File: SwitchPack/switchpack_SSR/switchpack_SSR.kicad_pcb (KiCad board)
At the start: 2 copper layers, 12 parts, among them J1 OUT_DIP_LEFT, J2 GND, J3 IN_DIP_LEFT, J4 GND, J5 VBAT_DIP_LEFT, U1 VN7003ALH

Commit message: Update switchpack
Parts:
- added C2: 100n, Yame_library:SM0402-MR, F.Cu at (126.2, -6.30)
- added C3: 100n, Yame_library:SM0402-MR, F.Cu at (133.0, -13.2)
- added C4: 100n, Yame_library:SM0402-MR, F.Cu at (144.9, -28.7)
- added C5: 100n, Yame_library:SM0402-MR, F.Cu at (149.3, -31.7)
- added C6: 100n, Yame_library:SM0402-MR, F.Cu at (128.6, -9.72)
- added C7: 100n, Yame_library:SM0402-MR, F.Cu at (133.0, -15.8)
- added C8: 22u, Yame_library:SM0805-MR, F.Cu at (186.1, -37.7)
- added D2: LED, LED_SMD:LED_0805_2012Metric, F.Cu at (128.7, -15.6)
- added D3: LED, LED_SMD:LED_0805_2012Metric, F.Cu at (145.0, -31.5)
- added D4: LED, LED_SMD:LED_0805_2012Metric, F.Cu at (128.7, -12.5)
- added D5: LED, LED_SMD:LED_0805_2012Metric, F.Cu at (133.2, -18.6)
- added D6: LED, LED_SMD:LED_0805_2012Metric, F.Cu at (128.7, -18.6)
- added D7: LED, LED_SMD:LED_0805_2012Metric, F.Cu at (137.6, -18.6)
- added D8: D_Schottky, Diode_SMD:D_SOD-123F, F.Cu at (186.8, -49.0)
- added J10: OUT_AC_REC, Connector_Wire:SolderWire-2.5sqmm_1x01_D2.4mm_OD4.4mm, F.Cu at (131.2, 103.5)
- added J11: IN_AC_REC, Connector_Pin:Pin_D0.7mm_L6.5mm_W1.8mm_FlatFork, F.Cu at (121.1, 112.4)
- added J12: VBAT_MB_LEFT, Connector_Wire:SolderWire-2.5sqmm_1x01_D2.4mm_OD4.4mm, F.Cu at (159.2, 72.0)
- added J13: VBAT_PARKING_LIGHT, Connector_Wire:SolderWire-2.5sqmm_1x01_D2.4mm_OD4.4mm, F.Cu at (141.8, 119.5)
- added J14: OUT_DIP_RIGHT, Connector_Wire:SolderWire-2.5sqmm_1x01_D2.4mm_OD4.4mm, F.Cu at (131.2, 128.4)
- added J15: OUT_MB_RIGHT, Connector_Wire:SolderWire-2.5sqmm_1x01_D2.4mm_OD4.4mm, F.Cu at (125.2, 74.7)
- added J16: OUT_FOG_LIGHT, Connector_Wire:SolderWire-2.5sqmm_1x01_D2.4mm_OD4.4mm, F.Cu at (136.9, 104.0)
- added J17: IN_DIP_RIGHT, Connector_Pin:Pin_D0.7mm_L6.5mm_W1.8mm_FlatFork, F.Cu at (121.1, 119.5)
- added J18: IN_MB_RIGHT, Connector_Pin:Pin_D0.7mm_L6.5mm_W1.8mm_FlatFork, F.Cu at (125.2, 80.7)
- added J19: IN_FOG_LIGHT, Connector_Pin:Pin_D0.7mm_L6.5mm_W1.8mm_FlatFork, F.Cu at (147.1, 112.8)
- added J20: VBAT_AC_REC, Connector_Wire:SolderWire-2.5sqmm_1x01_D2.4mm_OD4.4mm, F.Cu at (126.2, 112.4)
- added J21: VBAT_DIP_RIGHT, Connector_Wire:SolderWire-2.5sqmm_1x01_D2.4mm_OD4.4mm, F.Cu at (126.2, 119.5)
- added J22: VBAT_MB_RIGHT, Connector_Wire:SolderWire-2.5sqmm_1x01_D2.4mm_OD4.4mm, F.Cu at (137.2, 77.0)
- added J23: VBAT_FOG_LIGHT, Connector_Wire:SolderWire-2.5sqmm_1x01_D2.4mm_OD4.4mm, F.Cu at (142.1, 112.8)
- added J24: +3.3V, Connector_Pin:Pin_D0.7mm_L6.5mm_W1.8mm_FlatFork, F.Cu at (191.2, -13.6)
- added J25: +12V, Connector_Pin:Pin_D0.7mm_L6.5mm_W1.8mm_FlatFork, F.Cu at (196.6, -23.6)
- added J6: OUT_MB_LEFT, Connector_Wire:SolderWire-2.5sqmm_1x01_D2.4mm_OD4.4mm, F.Cu at (147.1, 69.7)
- added J7: OUT_PARKING_LIGHT, Connector_Wire:SolderWire-2.5sqmm_1x01_D2.4mm_OD4.4mm, F.Cu at (136.7, 128.4)
- added J8: IN_MB_LEFT, Connector_Pin:Pin_D0.7mm_L6.5mm_W1.8mm_FlatFork, F.Cu at (147.1, 75.7)
- added J9: IN_PARKING_LIGHT, Connector_Pin:Pin_D0.7mm_L6.5mm_W1.8mm_FlatFork, F.Cu at (146.8, 119.5)
- added Q1: DTC143Z, Package_TO_SOT_SMD:SOT-323_SC-70, F.Cu at (186.3, -40.9)
- added Q2: DTC143Z, Package_TO_SOT_SMD:SOT-323_SC-70, F.Cu at (191.1, -44.2)
- added Q3: DTC143Z, Package_TO_SOT_SMD:SOT-323_SC-70, F.Cu at (196.6, -48.8)
- added Q4: DTC143Z, Package_TO_SOT_SMD:SOT-323_SC-70, F.Cu at (190.7, -40.6)
- added Q5: DTC143Z, Package_TO_SOT_SMD:SOT-323_SC-70, F.Cu at (195.2, -40.6)
- added Q6: DTC143Z, Package_TO_SOT_SMD:SOT-323_SC-70, F.Cu at (201.1, -48.8)
- added Q7: DTC143Z, Package_TO_SOT_SMD:SOT-323_SC-70, F.Cu at (195.6, -44.2)
- added R10: 1k, Yame_library:SM0402-MR, F.Cu at (133.0, -10.6)
- added R11: 1k, Yame_library:SM0402-MR, F.Cu at (126.2, -3.68)
- added R12: 15k, Yame_library:SM0402-MR, F.Cu at (153.5, -31.7)
- added R13: 15k, Yame_library:SM0402-MR, F.Cu at (130.3, -7.10)
- added R14: 15k, Yame_library:SM0402-MR, F.Cu at (137.2, -13.2)
- added R15: 1k, Yame_library:SM0402-MR, F.Cu at (153.5, -29.1)
- added R16: 1k, Yame_library:SM0402-MR, F.Cu at (149.3, -29.1)
- added R17: 1k, Yame_library:SM0402-MR, F.Cu at (141.3, -15.8)
- added R18: 15k, Yame_library:SM0402-MR, F.Cu at (134.5, -7.94)
- added R19: 15k, Yame_library:SM0402-MR, F.Cu at (134.5, -5.32)
- added R20: 15k, Yame_library:SM0402-MR, F.Cu at (137.2, -15.8)
- added R21: 1k, Yame_library:SM0402-MR, F.Cu at (146.1, -18.2)
- added R22: 15k, Yame_library:SM0402-MR, F.Cu at (141.3, -13.2)
- added R23: 1k, Yame_library:SM0402-MR, F.Cu at (126.2, -1.06)
- added R24: 1k, Yame_library:SM0402-MR, F.Cu at (130.3, -4.48)
- added R25: 1k, Yame_library:SM0402-MR, F.Cu at (137.2, -10.6)
- added R26: 15k, Yame_library:SM0402-MR, F.Cu at (153.2, -26.5)
- added R27: 15k, Yame_library:SM0402-MR, F.Cu at (146.1, -20.8)
- added R28: 15k, Yame_library:SM0402-MR, F.Cu at (149.0, -23.9)
- added R29: 15k, Yame_library:SM0402-MR, F.Cu at (190.3, -37.4)
- added R30: 15k, Yame_library:SM0402-MR, F.Cu at (199.9, -45.7)
- added R31: 15k, Yame_library:SM0402-MR, F.Cu at (205.4, -49.3)
- added R32: 15k, Yame_library:SM0402-MR, F.Cu at (194.4, -37.4)
- added R33: 15k, Yame_library:SM0402-MR, F.Cu at (199.9, -43.1)
- added R34: 15k, Yame_library:SM0402-MR, F.Cu at (204.0, -45.7)
- added R35: 15k, Yame_library:SM0402-MR, F.Cu at (199.5, -40.4)
- added R5: 1k, Yame_library:SM0402-MR, F.Cu at (130.3, -1.86)
- added R6: 1k, Yame_library:SM0402-MR, F.Cu at (144.9, -26.1)
- added R7: 15k, Yame_library:SM0402-MR, F.Cu at (144.9, -23.5)
- added R8: 15k, Yame_library:SM0402-MR, F.Cu at (141.9, -18.8)
- added R9: 1k, Yame_library:SM0402-MR, F.Cu at (149.0, -26.5)
- added U2: VN7003ALH, Yame_library:VN7003ALH, B.Cu at (152.1, 82.8)
- added U3: VN7003ALH, Yame_library:VN7003ALH, B.Cu at (149.0, 128.2)
- added U4: VN7003ALH, Yame_library:VN7003ALH, B.Cu at (124.2, 103.8)
- added U5: VN7003ALH, Yame_library:VN7003ALH, B.Cu at (119.3, 127.5)
- added U6: VN7003ALH, Yame_library:VN7003ALH, B.Cu at (134.7, 87.8)
- added U7: VN7003ALH, Yame_library:VN7003ALH, B.Cu at (152.7, 105.7)
- C1, R1, R2, R3, R4: footprint Yame_library:SM0805-MR -> Yame_library:SM0402-MR
- J2, J4: footprint Connector_Wire:SolderWire-0.75sqmm_1x01_D1.25mm_OD2.3mm -> Connector_Pin:Pin_D0.7mm_L6.5mm_W1.8mm_FlatFork
- U1: moved to B.Cu
- moved J5 89.0 mm to (177.2, 80.3)
- moved U1 85.8 mm to (167.8, 82.5), turned to 90 degrees
- moved J1 78.6 mm to (168.3, 75.2)
- moved J3 76.8 mm to (177.2, 75.3)
- moved C1 59.9 mm to (169.5, 54.2)
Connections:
- R2 pad 2: Net-(J3-Pad1) -> +3V3
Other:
- board text added: "AC+"
- board text added: "ACin"
- board text added: "ACout"
- board text added: "B-"
- board text added: "DipL"
- board text added: "DipLin"
- board text added: "DipLout"
- board text added: "DipR"
- board text added: "DipRIn"
- board text added: "DipRout"
- board text added: "Fog+"
- board text added: "FogIn"
- board text added: "FogOut"
- board text added: "MBL+"
- board text added: "MBLin"
- board text added: "MBLout"
- board text added: "MBR+"
- board text added: "MBRin"
- board text added: "MBRout"
- board text added: "Park+"
- board text added: "Parkin"
- board text added: "Parkout"

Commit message: SwitchPack : update layout
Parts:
- removed D8: D_Schottky, Diode_SMD:D_SOD-123F
- added R36: 0R, Yame_library:SM0402-MR, F.Cu at (202.8, 103.0)
- C5, R23, R26: moved to B.Cu
- moved Q3 199.5 mm to (142.9, 143.3)
- moved R31 193.1 mm to (146.7, 134.7)
- moved R33 178.4 mm to (121.1, 117.0), turned to 90 degrees
- moved Q5 177.6 mm to (115.9, 118.4), turned to 180 degrees
- moved D3 169.6 mm to (147.3, 138.1)
- moved C5 165.1 mm to (124.6, 131.6)
- moved R6 163.5 mm to (140.6, 137.3)
- moved R15 162.7 mm to (132.8, 132.3), turned to 180 degrees
- moved C3 158.8 mm to (153.3, 144.3)
- moved R26 158.1 mm to (127.2, 129.4)
- moved D5 150.8 mm to (129.7, 132.2)
- moved J25 148.9 mm to (136.9, 112.8)
- moved R11 143.0 mm to (154.9, 136.4)
- moved R13 142.6 mm to (156.7, 133.1)
- moved J24 140.3 mm to (152.1, 121.1)
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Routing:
- net Net-(C3-Pad1): track 0.00 -> 14.8 mm
- net Net-(C5-Pad1): track 0.00 -> 14.4 mm
- net Net-(J7-Pad1): track 0.00 -> 12.9 mm
- net Net-(J14-Pad1): track 0.00 -> 9.50 mm
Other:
- board outline added: 68.2 x 78.8 mm
- copper layers 2 -> 4

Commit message: switchpack : update layout
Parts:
- C1, C2, C3, C4, C6, C7, R10, R11, R12, R13, R21, R22, R24, R25, R27, R28, R3, R4: moved to B.Cu
- moved Q4 170.4 mm to (116.9, 113.0), turned to 180 degrees
- moved R32 169.2 mm to (119.0, 114.1), turned to 270 degrees
- moved Q7 164.3 mm to (151.1, 114.0)
- moved R35 161.5 mm to (148.9, 113.0), turned to 90 degrees
- moved C8 161.4 mm to (157.4, 121.0)
- moved Q6 156.7 mm to (120.8, 85.8)
- moved R34 155.9 mm to (118.6, 84.7), turned to 90 degrees
- moved C4 137.4 mm to (129.6, 107.8)
- moved R30 136.4 mm to (142.1, 77.8), turned to 90 degrees
- moved R9 135.4 mm to (133.2, 108.0), turned to 270 degrees
- moved Q2 131.8 mm to (144.2, 79.0)
- moved R20 131.2 mm to (153.2, 114.5), turned to 270 degrees
- moved D7 128.8 mm to (135.8, 110.2), turned to 180 degrees
- moved J2 128.0 mm to (175.1, 119.9)
- moved R14 127.7 mm to (114.7, 112.5), turned to 90 degrees
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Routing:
- net +12V: track 0.00 -> 182.3 mm
- net +3V3: track 0.00 -> 176.9 mm, vias 0 -> 4
- net GND: track 0.00 -> 73.7 mm, vias 0 -> 31
- net Net-(J16-Pad1): track 0.00 -> 29.3 mm
- net Net-(J1-Pad1): track 0.00 -> 25.8 mm
- net Net-(J10-Pad1): track 0.00 -> 25.6 mm
- net Net-(C2-Pad1): track 0.00 -> 22.3 mm, vias 0 -> 64
- net Net-(C6-Pad1): track 0.00 -> 22.3 mm, vias 0 -> 64
- net Net-(Q5-Pad3): track 0.00 -> 21.6 mm, vias 0 -> 1
- net Net-(C1-Pad1): track 0.00 -> 21.5 mm, vias 0 -> 64
- net Net-(C4-Pad1): track 0.00 -> 21.3 mm, vias 0 -> 64
- net Net-(C7-Pad1): track 0.00 -> 21.1 mm, vias 0 -> 64
- net Net-(Q7-Pad3): track 0.00 -> 21.0 mm, vias 0 -> 1
- net Net-(Q4-Pad3): track 0.00 -> 20.6 mm, vias 0 -> 1
- net Net-(J6-Pad1): track 0.00 -> 20.6 mm
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- added copper zone on B.Cu, net GND
- added copper zone on F.Cu, net GND
- added copper zone on B.Cu, net Net-(C1-Pad1)
- added copper zone on F.Cu, net Net-(C1-Pad1)
- added copper zone on B.Cu, net Net-(C2-Pad1)
- added copper zone on F.Cu, net Net-(C2-Pad1)
- added copper zone on B.Cu, net Net-(C3-Pad1)
- added copper zone on F.Cu, net Net-(C3-Pad1)
- added copper zone on B.Cu, net Net-(C4-Pad1)
- added copper zone on F.Cu, net Net-(C4-Pad1)
- added copper zone on B.Cu, net Net-(C5-Pad1)
- added copper zone on F.Cu, net Net-(C5-Pad1)
- added copper zone on B.Cu, net Net-(C6-Pad1)
- added copper zone on F.Cu, net Net-(C6-Pad1)
- added copper zone on B.Cu, net Net-(C7-Pad1)
- added copper zone on F.Cu, net Net-(C7-Pad1)
- added copper zone on B.Cu, net Net-(J1-Pad1)
- added copper zone on B.Cu, net Net-(J10-Pad1)
- added copper zone on B.Cu, net Net-(J14-Pad1)
- added copper zone on B.Cu, net Net-(J15-Pad1)
- added copper zone on B.Cu, net Net-(J16-Pad1)
- added copper zone on B.Cu, net Net-(J6-Pad1)
- added copper zone on B.Cu, net Net-(J7-Pad1)
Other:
- copper layers 4 -> 2
- net class Default: clearance 0.2 -> 0.15; trace_width 0.25 -> 0.15; via_dia 0.8 -> 0.4; via_drill 0.4 -> 0.2
- rule trace_clearance: 0.2 -> 0.15
- rule trace_min: 0.2 -> 0.15
- rule via_min_drill: 0.3 -> 0.1
- rule via_min_size: 0.4 -> 0.2

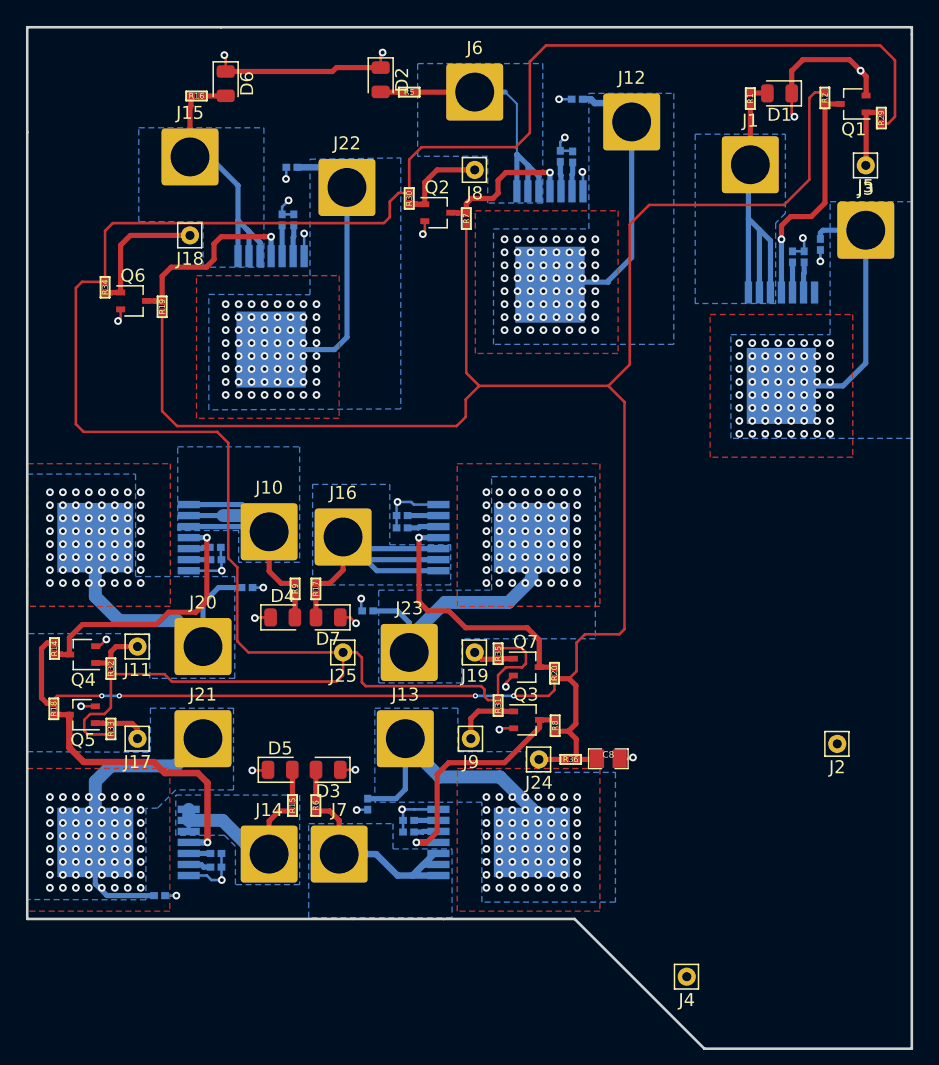
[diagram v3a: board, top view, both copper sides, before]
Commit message: switchpack : update layout
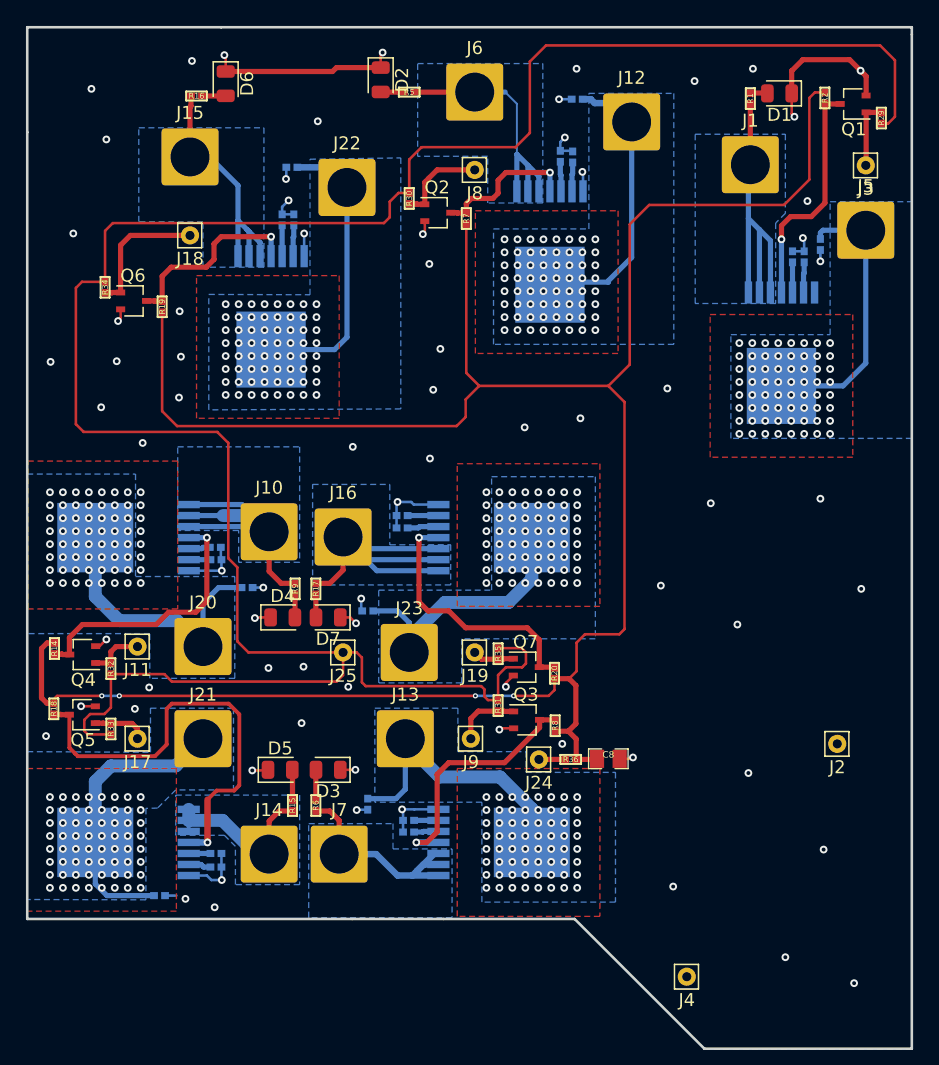
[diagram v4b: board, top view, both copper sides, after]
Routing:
- net Net-(Q5-Pad3): track 21.6 -> 33.9 mm
- net GND: vias 31 -> 74

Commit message: Update Gas sensor
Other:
- net class Default removed
